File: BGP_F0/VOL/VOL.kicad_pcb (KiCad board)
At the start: 2 copper layers, 20 x 26 mm, 3 parts, among them P1 CONN_01X02

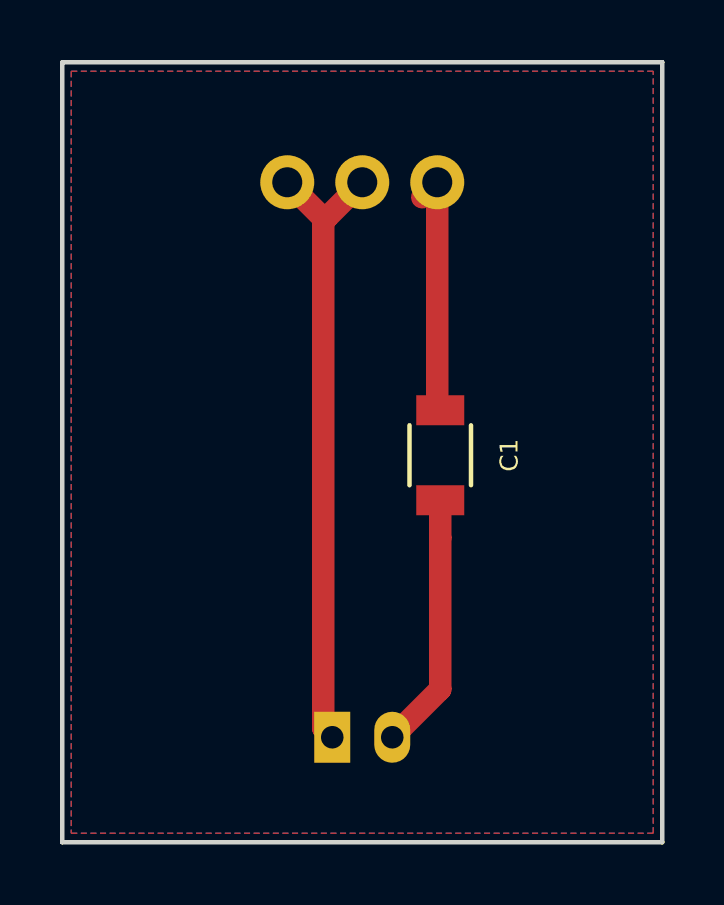
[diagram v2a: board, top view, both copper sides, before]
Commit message: Tone cap changed to female pin strip header for 0.047uF and 0.1uF
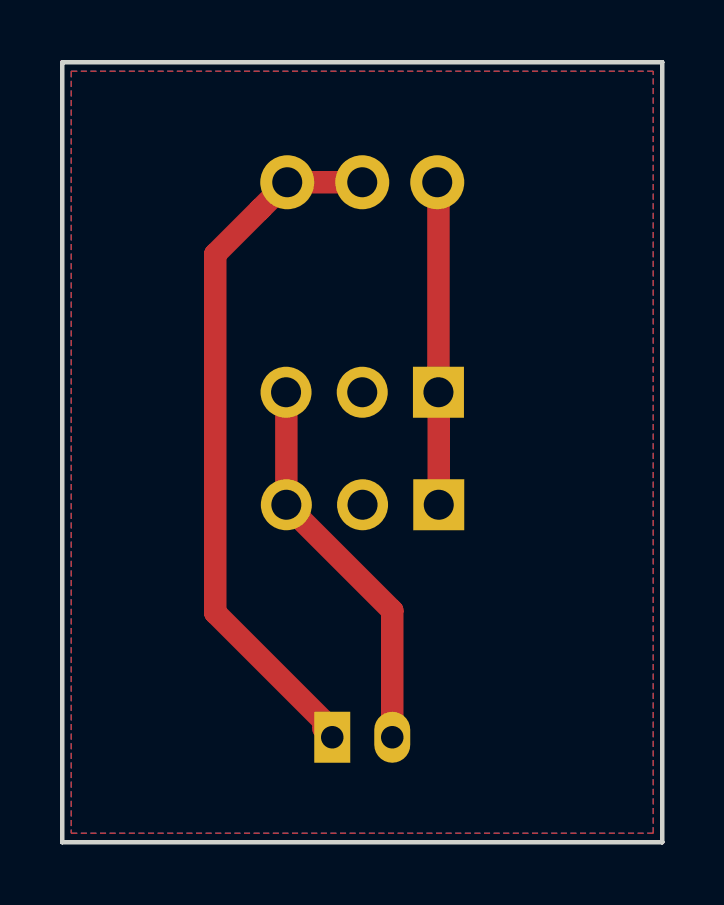
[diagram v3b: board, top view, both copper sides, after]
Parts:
- removed C1: 47n, Capacitors_SMD:C_1206
- added J1: Conn_01x03_Female, Pin_Headers:Pin_Header_Straight_1x03_Pitch2.54mm, B.Cu at (150.5, 87.0)
- added J2: Conn_01x03_Female, Pin_Headers:Pin_Header_Straight_1x03_Pitch2.54mm, B.Cu at (150.6, 90.8)
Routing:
- net /VOL_3: track 8.56 -> 13.0 mm
- net Net-(J1-Pad1): track 8.35 -> 10.8 mm
- net /VOL_1: track 21.6 -> 24.0 mm

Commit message: Mid Buff
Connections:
- RV1 pad 2: /VOL_1 -> Net-(J1-Pad1)
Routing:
- net Net-(J1-Pad1): track 10.8 -> 13.3 mm
- net /VOL_1: track 24.0 -> 22.7 mm
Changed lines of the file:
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@@
   (general
     (links 6)
-    (no_connects 6)
+    (no_connects 0)
     (area 137.924999 75.924999 158.075001 102.075001)
     (thickness 1.6)
@@
       (net 3 "Net-(J1-Pad1)"))
     (pad 2 thru_hole circle (at 0 2.5 90) (size 1.8 1.8) (drill 1) (layers *.Cu *.Mask)
-      (net 1 /VOL_1))
+      (net 3 "Net-(J1-Pad1)"))
     (pad 1 thru_hole circle (at 0 0 90) (size 1.8 1.8) (drill 1) (layers *.Cu *.Mask)
       (net 1 /VOL_1))
@@
   (gr_line (start 138 76) (end 138 102) (layer Edge.Cuts) (width 0.15))
   (gr_line (start 158 76) (end 138 76) (layer Edge.Cuts) (width 0.15))
+  (segment (start 143 95.85) (end 143 82.5) (width 0.75) (layer F.Cu) (net 1))
+  (segment (start 143 82.5) (end 145.5 80) (width 0.75) (layer F.Cu) (net 1))
+  (segment (start 147 98.5) (end 145.65 98.5) (width 0.75) (layer F.Cu) (net 1))
+  (segment (start 145.65 98.5) (end 143 95.85) (width 0.75) (layer F.Cu) (net 1))
   (segment (start 147 98.5) (end 147 98.25) (width 0.75) (layer F.Cu) (net 1))
-  (segment (start 147 98.25) (end 143.1 94.35) (width 0.75) (layer F.Cu) (net 1))
-  (segment (start 143.1 94.35) (end 143.1 82.4) (width 0.75) (layer F.Cu) (net 1))
-  (segment (start 143.1 82.4) (end 144.600001 80.899999) (width 0.75) (layer F.Cu) (net 1))
-  (segment (start 144.600001 80.899999) (end 145.5 80) (width 0.75) (layer F.Cu) (net 1))
-  (segment (start 145.5 80) (end 148 80) (width 0.75) (layer F.Cu) (net 1))
   (segment (start 147 98.5) (end 146.7 98.2) (width 0.75) (layer F.Cu) (net 1))
   (segment (start 145.47 90.75) (end 145.47 87.01) (width 0.75) (layer F.Cu) (net 2))
@@
   (segment (start 149 98.5) (end 149 94.28) (width 0.75) (layer F.Cu) (net 2))
   (segment (start 149 94.28) (end 145.47 90.75) (width 0.75) (layer F.Cu) (net 2))
+  (segment (start 150.5 80) (end 148 80) (width 0.75) (layer F.Cu) (net 3))
   (segment (start 150.54 87) (end 150.54 80.04) (width 0.75) (layer F.Cu) (net 3))
   (segment (start 150.54 80.04) (end 150.5 80) (width 0.75) (layer F.Cu) (net 3))

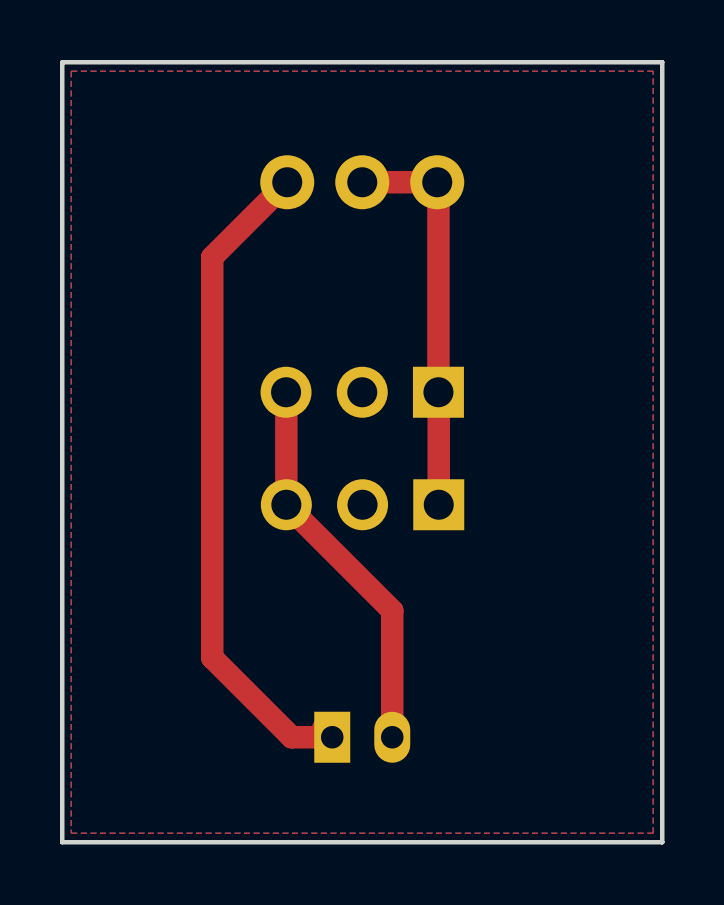
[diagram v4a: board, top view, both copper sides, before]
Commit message: Tone pot 20k
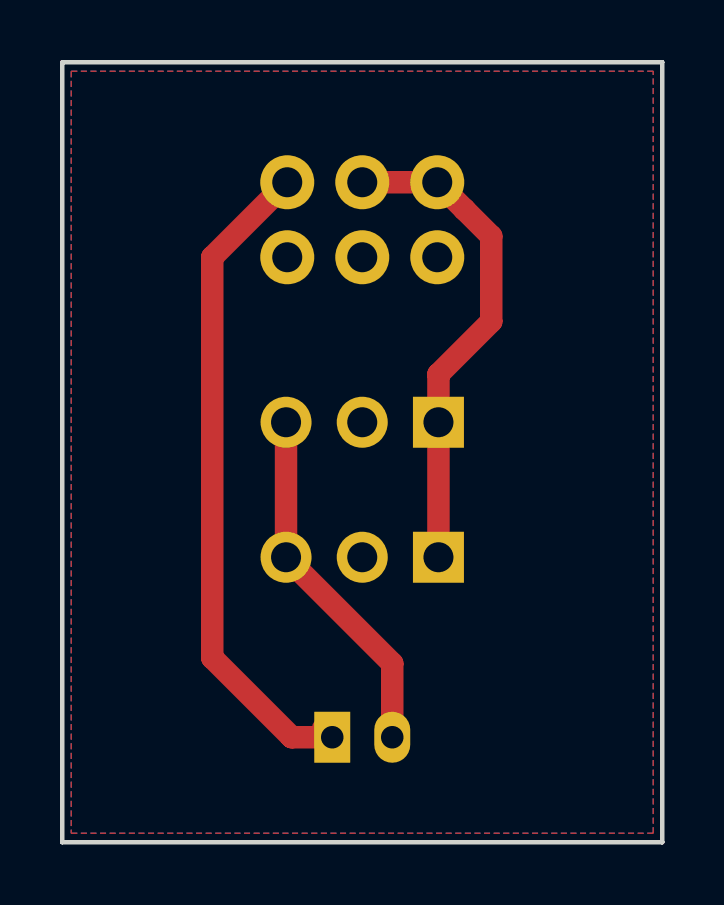
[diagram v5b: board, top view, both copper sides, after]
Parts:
- RV1: footprint LIBS:Potentiometer_Alps_RK097_Single_Vertical -> LIBS:Potentiometer_Alps_RK097_Double_Vertical
- moved J2 1.75 mm to (150.5, 92.5)
- moved J1 1.00 mm to (150.5, 88.0)
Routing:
- net Net-(J1-Pad1): track 13.3 -> 16.5 mm
- net /VOL_3: track 13.0 -> 12.0 mm
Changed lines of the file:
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@@
   (general
     (links 6)
-    (no_connects 0)
+    (no_connects 4)
     (area 137.924999 75.924999 158.075001 102.075001)
     (thickness 1.6)
     (drawings 8)
-    (tracks 15)
+    (tracks 17)
     (zones 0)
     (modules 4)
@@
     (add_net "Net-(J2-Pad2)")
   )
-  (module LIBS:Potentiometer_Alps_RK097_Single_Vertical (layer B.Cu)
-    (at 145.5 80 90)
-    (descr "Potentiometer, vertically mounted, Omeg PC16PU, Omeg PC16PU, Omeg PC16PU, Vishay/Spectrol 248GJ/249GJ Single, Vishay/Spectrol 248GJ/249GJ Single, Vishay/Spectrol 248GJ/249GJ Single, Vishay/Spectrol 248GH/249GH Single, Vishay/Spectrol 148/149 Single, Vishay/Spectrol 148/149 Single, Vishay/Spectrol 148/149 Single, Vishay/Spectrol 148A/149A Single with mounting plates, Vishay/Spectrol 148/149 Double, Vishay/Spectrol 148A/149A Double with mounting plates, Piher PC-16 Single, Piher PC-16 Single, Piher PC-16 Single, Piher PC-16SV Single, Piher PC-16 Double, Piher PC-16 Triple, Piher T16H Single, Piher T16L Single, Piher T16H Double, Alps RK163 Single, Alps RK163 Double, Alps RK097 Single, http://www.alps.com/prod/info/E/HTML/Potentiometer/RotaryPotentiometers/RK097/RK097111080J.html")
-    (tags "Potentiometer vertical  Omeg PC16PU  Omeg PC16PU  Omeg PC16PU  Vishay/Spectrol 248GJ/249GJ Single  Vishay/Spectrol 248GJ/249GJ Single  Vishay/Spectrol 248GJ/249GJ Single  Vishay/Spectrol 248GH/249GH Single  Vishay/Spectrol 148/149 Single  Vishay/Spectrol 148/149 Single  Vishay/Spectrol 148/149 Single  Vishay/Spectrol 148A/149A Single with mounting plates  Vishay/Spectrol 148/149 Double  Vishay/Spectrol 148A/149A Double with mounting plates  Piher PC-16 Single  Piher PC-16 Single  Piher PC-16 Single  Piher PC-16SV Single  Piher PC-16 Double  Piher PC-16 Triple  Piher T16H Single  Piher T16L Single  Piher T16H Double  Alps RK163 Single  Alps RK163 Double  Alps RK097 Single")
-    (fp_text reference RV1 (at 0 7.9 90) (layer B.SilkS)
-      (effects (font (size 0.6 0.6) (thickness 0.15)) (justify mirror))
-    )
-    (fp_text value POT (at 0 -3.5 90) (layer B.Fab) hide
-      (effects (font (size 0.6 0.6) (thickness 0.15)) (justify mirror))
-    )
-    (fp_line (start -2.05 7.25) (end -2.05 -2.25) (layer B.Fab) (width 0.1))
-    (fp_line (start -2.05 -2.25) (end 2 -2.25) (layer B.Fab) (width 0.1))
-    (fp_line (start 2 -2.25) (end 2 7.25) (layer B.Fab) (width 0.1))
-    (fp_line (start 2 7.25) (end -2.05 7.25) (layer B.Fab) (width 0.1))
-    (fp_line (start -2.11 7.31) (end 2.06 7.31) (layer B.SilkS) (width 0.12))
-    (fp_line (start -2.11 -2.31) (end 2.06 -2.31) (layer B.SilkS) (width 0.12))
-    (fp_line (start -2.11 7.31) (end -2.11 -2.31) (layer B.SilkS) (width 0.12))
-    (fp_line (start 2.06 7.31) (end 2.06 -2.31) (layer B.SilkS) (width 0.12))
-    (fp_line (start -2.3 7.5) (end -2.3 -2.5) (layer B.CrtYd) (width 0.05))
-    (fp_line (start -2.3 -2.5) (end 2.25 -2.5) (layer B.CrtYd) (width 0.05))
-    (fp_line (start 2.25 -2.5) (end 2.25 7.5) (layer B.CrtYd) (width 0.05))
-    (fp_line (start 2.25 7.5) (end -2.3 7.5) (layer B.CrtYd) (width 0.05))
-    (pad 3 thru_hole circle (at 0 5 90) (size 1.8 1.8) (drill 1) (layers *.Cu *.Mask)
-      (net 3 "Net-(J1-Pad1)"))
-    (pad 2 thru_hole circle (at 0 2.5 90) (size 1.8 1.8) (drill 1) (layers *.Cu *.Mask)
-      (net 3 "Net-(J1-Pad1)"))
-    (pad 1 thru_hole circle (at 0 0 90) (size 1.8 1.8) (drill 1) (layers *.Cu *.Mask)
-      (net 1 /VOL_1))
-    (model Potentiometers.3dshapes/Potentiometer_Alps_RK097_Single_Vertical.wrl
-      (at (xyz 0 0 0))
-      (scale (xyz 0.393701 0.393701 0.393701))
-      (rotate (xyz 0 0 0))
-    )
-  )
   (module Connectors_JST:JST_PH_B2B-PH-K_02x2.00mm_Straight (layer B.Cu)
     (at 147 98.5)
@@
   )
   (module Pin_Headers:Pin_Header_Straight_1x03_Pitch2.54mm (layer B.Cu)
-    (at 150.54 87 90)
+    (at 150.54 88 90)
     (descr "Through hole straight pin header, 1x03, 2.54mm pitch, single row")
     (tags "Through hole pin header THT 1x03 2.54mm single row")
@@
   )
   (module Pin_Headers:Pin_Header_Straight_1x03_Pitch2.54mm (layer B.Cu)
-    (at 150.55 90.75 90)
+    (at 150.54 92.5 90)
     (descr "Through hole straight pin header, 1x03, 2.54mm pitch, single row")
     (tags "Through hole pin header THT 1x03 2.54mm single row")
@@
     )
   )
+  (module LIBS:Potentiometer_Alps_RK097_Double_Vertical (layer B.Cu)
+    (at 145.5 80 90)
+    (descr "Potentiometer, vertically mounted, Omeg PC16PU, Omeg PC16PU, Omeg PC16PU, Vishay/Spectrol 248GJ/249GJ Single, Vishay/Spectrol 248GJ/249GJ Single, Vishay/Spectrol 248GJ/249GJ Single, Vishay/Spectrol 248GH/249GH Single, Vishay/Spectrol 148/149 Single, Vishay/Spectrol 148/149 Single, Vishay/Spectrol 148/149 Single, Vishay/Spectrol 148A/149A Single with mounting plates, Vishay/Spectrol 148/149 Double, Vishay/Spectrol 148A/149A Double with mounting plates, Piher PC-16 Single, Piher PC-16 Single, Piher PC-16 Single, Piher PC-16SV Single, Piher PC-16 Double, Piher PC-16 Triple, Piher T16H Single, Piher T16L Single, Piher T16H Double, Alps RK163 Single, Alps RK163 Double, Alps RK097 Single, Alps RK097 Double, http://www.alps.com/prod/info/E/HTML/Potentiometer/RotaryPotentiometers/RK097/RK09712100AV.html")
+    (tags "Potentiometer vertical  Omeg PC16PU  Omeg PC16PU  Omeg PC16PU  Vishay/Spectrol 248GJ/249GJ Single  Vishay/Spectrol 248GJ/249GJ Single  Vishay/Spectrol 248GJ/249GJ Single  Vishay/Spectrol 248GH/249GH Single  Vishay/Spectrol 148/149 Single  Vishay/Spectrol 148/149 Single  Vishay/Spectrol 148/149 Single  Vishay/Spectrol 148A/149A Single with mounting plates  Vishay/Spectrol 148/149 Double  Vishay/Spectrol 148A/149A Double with mounting plates  Piher PC-16 Single  Piher PC-16 Single  Piher PC-16 Single  Piher PC-16SV Single  Piher PC-16 Double  Piher PC-16 Triple  Piher T16H Single  Piher T16L Single  Piher T16H Double  Alps RK163 Single  Alps RK163 Double  Alps RK097 Single  Alps RK097 Double")
+    (fp_text reference RV1 (at 0 8.5 90) (layer B.SilkS)
+      (effects (font (size 0.6 0.6) (thickness 0.15)) (justify mirror))
+    )
+    (fp_text value POT (at 0 -3.5 90) (layer B.Fab) hide
+      (effects (font (size 0.6 0.6) (thickness 0.15)) (justify mirror))
+    )
+    (fp_line (start -4.55 7.25) (end -4.55 -2.25) (layer B.Fab) (width 0.1))
+    (fp_line (start -4.55 -2.25) (end 4 -2.25) (layer B.Fab) (width 0.1))
+    (fp_line (start 4 -2.25) (end 4 7.25) (layer B.Fab) (width 0.1))
+    (fp_line (start 4 7.25) (end -4.55 7.25) (layer B.Fab) (width 0.1))
+    (fp_line (start -4.61 7.31) (end 4.06 7.31) (layer B.SilkS) (width 0.12))
+    (fp_line (start -4.61 -2.31) (end 4.06 -2.31) (layer B.SilkS) (width 0.12))
+    (fp_line (start -4.61 7.31) (end -4.61 -2.31) (layer B.SilkS) (width 0.12))
+    (fp_line (start 4.06 7.31) (end 4.06 -2.31) (layer B.SilkS) (width 0.12))
+    (fp_line (start -4.85 7.5) (end -4.85 -2.5) (layer B.CrtYd) (width 0.05))
+    (fp_line (start -4.85 -2.5) (end 4.5 -2.5) (layer B.CrtYd) (width 0.05))
+    (fp_line (start 4.5 -2.5) (end 4.5 7.5) (layer B.CrtYd) (width 0.05))
+    (fp_line (start 4.5 7.5) (end -4.85 7.5) (layer B.CrtYd) (width 0.05))
+    (pad 3 thru_hole circle (at 0 5 90) (size 1.8 1.8) (drill 1) (layers *.Cu *.Mask)
+      (net 3 "Net-(J1-Pad1)"))
+    (pad 2 thru_hole circle (at 0 2.5 90) (size 1.8 1.8) (drill 1) (layers *.Cu *.Mask)
+      (net 3 "Net-(J1-Pad1)"))
+    (pad 1 thru_hole circle (at 0 0 90) (size 1.8 1.8) (drill 1) (layers *.Cu *.Mask)
+      (net 1 /VOL_1))
+    (pad 6 thru_hole circle (at -2.5 5 90) (size 1.8 1.8) (drill 1) (layers *.Cu *.Mask))
+    (pad 5 thru_hole circle (at -2.5 2.5 90) (size 1.8 1.8) (drill 1) (layers *.Cu *.Mask))
+    (pad 4 thru_hole circle (at -2.5 0 90) (size 1.8 1.8) (drill 1) (layers *.Cu *.Mask))
+    (model Potentiometers.3dshapes/Potentiometer_Alps_RK097_Double_Vertical.wrl
+      (at (xyz 0 0 0))
+      (scale (xyz 0.393701 0.393701 0.393701))
+      (rotate (xyz 0 0 0))
+    )
+  )
   (gr_line (start 157.7 101.7) (end 157.7 76.3) (layer Margin) (width 0.2))
   (gr_line (start 138.3 101.7) (end 157.7 101.7) (layer Margin) (width 0.2))
@@
   (segment (start 147 98.5) (end 147 98.25) (width 0.75) (layer F.Cu) (net 1))
   (segment (start 147 98.5) (end 146.7 98.2) (width 0.75) (layer F.Cu) (net 1))
-  (segment (start 145.47 90.75) (end 145.47 87.01) (width 0.75) (layer F.Cu) (net 2))
-  (segment (start 145.47 87.01) (end 145.46 87) (width 0.75) (layer F.Cu) (net 2))
-  (segment (start 149 98.5) (end 149 94.28) (width 0.75) (layer F.Cu) (net 2))
-  (segment (start 149 94.28) (end 145.47 90.75) (width 0.75) (layer F.Cu) (net 2))
+  (segment (start 145.46 92.5) (end 145.46 88) (width 0.75) (layer F.Cu) (net 2))
+  (segment (start 149 98.5) (end 149 96.04) (width 0.75) (layer F.Cu) (net 2))
+  (segment (start 149 96.04) (end 145.46 92.5) (width 0.75) (layer F.Cu) (net 2))
+  (segment (start 150.54 88) (end 150.54 86.4) (width 0.75) (layer F.Cu) (net 3))
+  (segment (start 150.54 86.4) (end 152.3 84.64) (width 0.75) (layer F.Cu) (net 3))
+  (segment (start 152.3 84.64) (end 152.3 81.8) (width 0.75) (layer F.Cu) (net 3))
+  (segment (start 152.3 81.8) (end 151.399999 80.899999) (width 0.75) (layer F.Cu) (net 3))
+  (segment (start 151.399999 80.899999) (end 150.5 80) (width 0.75) (layer F.Cu) (net 3))
+  (segment (start 150.54 92.5) (end 150.54 88) (width 0.75) (layer F.Cu) (net 3))
   (segment (start 150.5 80) (end 148 80) (width 0.75) (layer F.Cu) (net 3))
-  (segment (start 150.54 87) (end 150.54 80.04) (width 0.75) (layer F.Cu) (net 3))
   (segment (start 150.54 80.04) (end 150.5 80) (width 0.75) (layer F.Cu) (net 3))
-  (segment (start 150.55 90.75) (end 150.55 87.01) (width 0.75) (layer F.Cu) (net 3))
-  (segment (start 150.55 87.01) (end 150.54 87) (width 0.75) (layer F.Cu) (net 3))
   (zone (net 0) (net_name "") (layer B.Cu) (hatch edge 0.508)
     (connect_pads (clearance 0.3))
